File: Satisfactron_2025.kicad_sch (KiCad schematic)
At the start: 93 parts, among them J10 Conn_01x02, J11 Conn_01x03, J17 Conn_01x02, J18 Conn_01x02, J19 Conn_01x02, J4 65100516121, J5 Conn_01x05, J6 Conn_01x06, J7 Conn_01x02, J8 Conn_01x04, J9 Conn_01x02, Q2 G2302, SW1 SW_DPST_x2, SW2 SW_Push, SW5 SW_Push, SW6 SW_Push, SW7 SW_Push, U1 AMS1117-3.3, U2 TPS82130, U3 ESP32-S3-WROOM-1-N16R8

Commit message: Start populate schematics
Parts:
- removed C1, C24, C3, C5, C6: 100nF, Capacitor_SMD:C_0603_1608Metric_Pad1.08x0.95mm_HandSolder, symbol Device:C
- removed J10, J17, J18, J19, J9: Conn_01x02, Connector_PinHeader_2.54mm:PinHeader_1x02_P2.54mm_Vertical, symbol Connector_Generic:Conn_01x02
- removed J4: 65100516121, ConnectorsEvo:USB_Mini-B_Wuerth_65100516121_Horizontal, symbol Connector:USB_B_Mini
- removed J5: Conn_01x05, Connector_PinHeader_2.54mm:PinHeader_1x05_P2.54mm_Vertical, symbol Connector_Generic:Conn_01x05
- removed J7: Conn_01x02, Connector_Wire:SolderWire-0.75sqmm_1x02_P4.8mm_D1.25mm_OD2.3mm, symbol Connector_Generic:Conn_01x02
- removed R21, R22, R4, R5, R8: 10k, Resistor_SMD:R_0603_1608Metric_Pad0.98x0.95mm_HandSolder, symbol Device:R
- removed SW1: SW_DPST_x2, SW_Slide_SPDT_Straight_CK_OS102011MS2Q, symbol Switch:SW_SPDT_321
- added H10, H11, H12, H13, H14, H15, H16, H17, H18, H19, H5, H6, H7, H8, H9: SMTSO3040CTJ, Fastener_KSL:SMD-1_BD5.5-D4.0, symbol Fastener_KSL:SMTSO3040CTJ
- added J1: USB-TYPE-C-018, Connector_KSL:USB-C_SMD-TYPE-C-31-M-12, symbol Connector_KSL:USB-TYPE-C-018
- added J2: GT-BTP30002-0350B-019B, Connector_KSL:CONN-SMD_GT-BTP30002-0350B-019B, symbol Connector_KSL:GT-BTP30002-0350B-019B
- added SW1: SS-12D11G5R, Switch_KSL:SW-TH_SS-12D11G5R, symbol Switch_KSL:SS-12D11G5R
- added SW10, SW3, SW4, SW8, SW9: SPVN310101, Switch_KSL:SW-SMD_SPVN310101, symbol Switch_KSL:SPVN310101
- added U4, U5, U6, U7, U8: TSSP77038TR, Sensor_KSL:SENSOR-SMD_TSOP75238TR, symbol Sensor_KSL:TSSP77038TR
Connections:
- no-connect marks 8 -> 24
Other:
- note added: "Battery input (Canon LP-E17, 7.4V), main switch"
- note added: "IR reflective sensors"
- note added: "Mechanical"
- note added: "Micro-switches"
- note added: "USB input"
- note removed: "+ switch principal"
- note removed: "5V USB non connecté, utiliser avec PAMI sous tension"
- note removed: "Capteur fin de course (NC)"
- note removed: "Capteur infrarouge"
- note removed: "Entree batterie LP-E6P 7.4V"
- note removed: "Entree: USB"
- note removed: "ajouter capteur IR: C499566"
- note removed: "conn. 'USB' dupont"
- note removed: "rempl par pogo batterie"
- moved on the sheet: C8

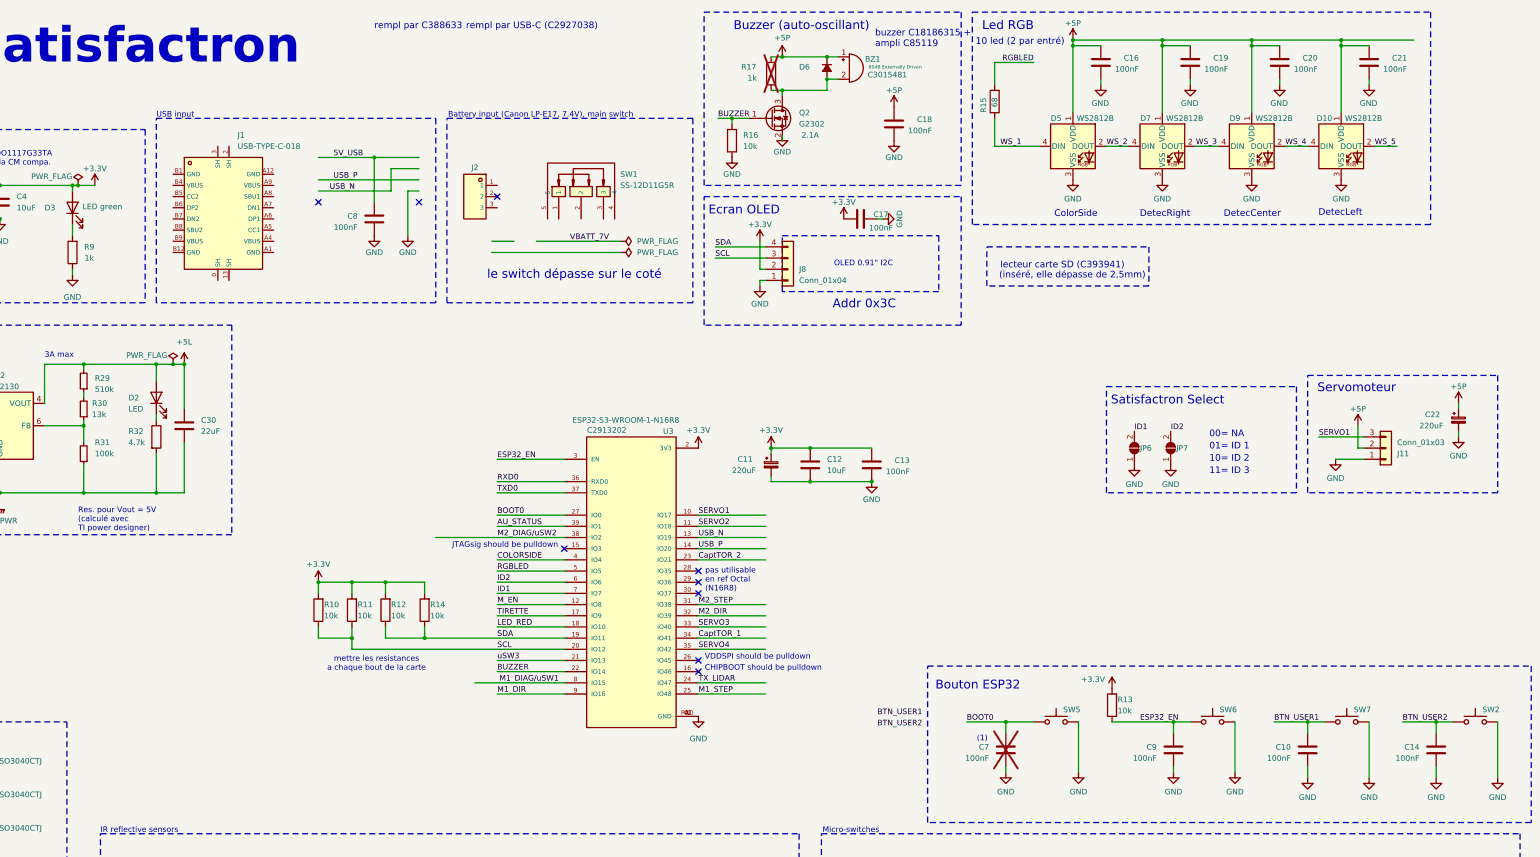
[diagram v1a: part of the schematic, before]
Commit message: Add DXF, sch placement + start PCB placement
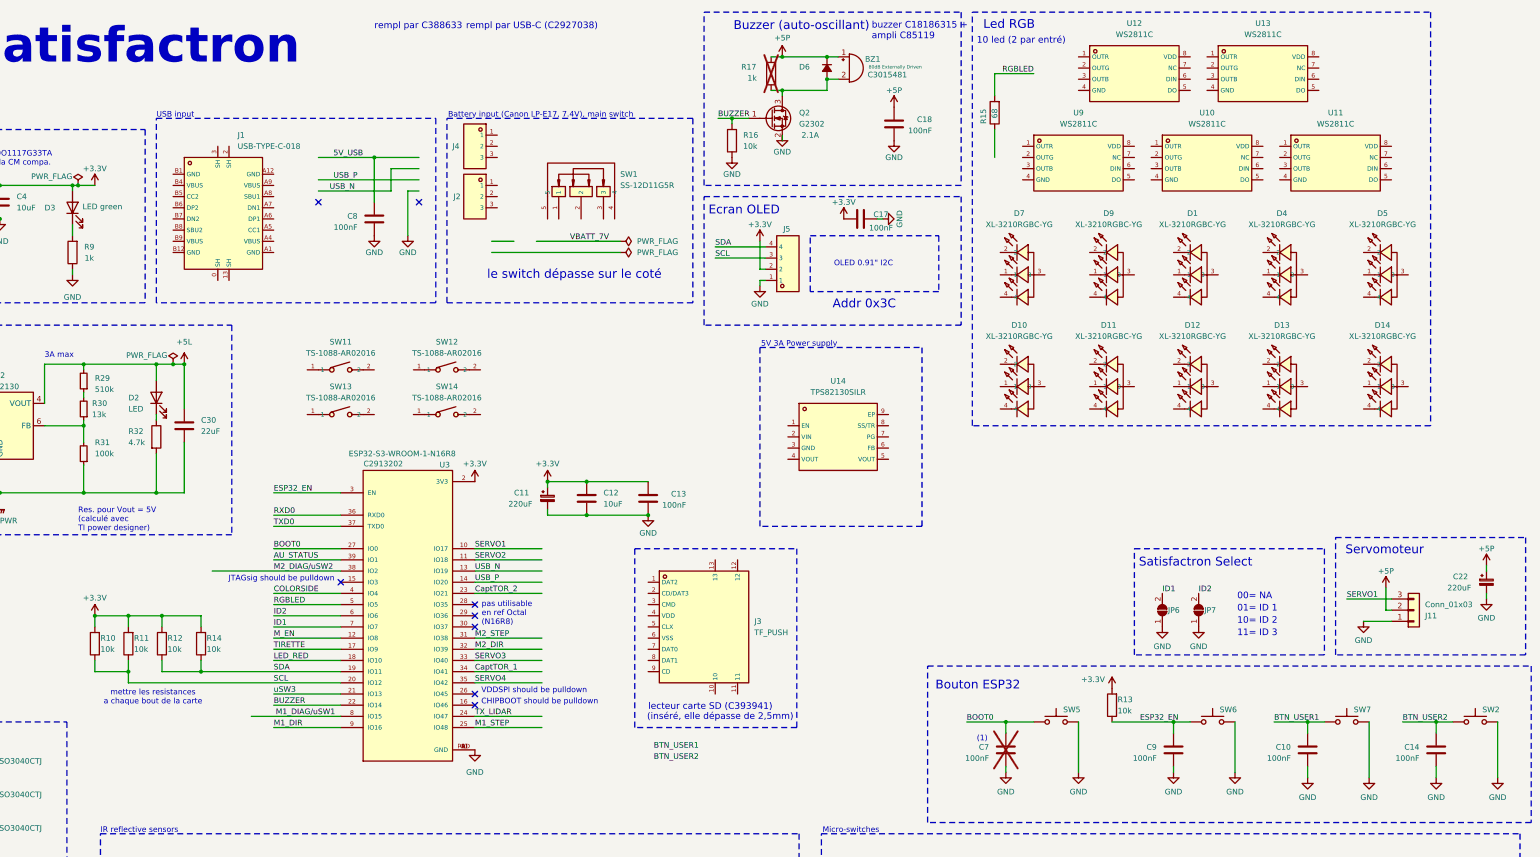
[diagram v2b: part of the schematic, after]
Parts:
- removed C16, C19, C20, C21: 100nF, Capacitor_SMD:C_0603_1608Metric_Pad1.08x0.95mm_HandSolder, symbol Device:C
- removed D10, D5, D7, D9: WS2812B, LED_SMD:LED_WS2812B_PLCC4_5.0x5.0mm_P3.2mm, symbol LED:WS2812B
- removed J8: Conn_01x04, Carte_Mere_PAMI_2025:Ecran_OLED0.9_Waveshare, symbol Connector_Generic:Conn_01x04
- added D1, D10, D11, D12, D13, D14, D4, D5, D7, D9: XL-3210RGBC-YG, LED_KSL:LED-ARRAY-SMD_HS-1204-RGB, symbol LED_KSL:XL-3210RGBC-YG
- added J3: TF_PUSH, Connector_KSL:TF-SMD_TF-PUSH, symbol Connector_KSL:TF_PUSH
- added J4: GT-BTP30002-0350B-019B, Connector_KSL:CONN-SMD_GT-BTP30002-0350B-019B, symbol Connector_KSL:GT-BTP30002-0350B-019B
- added J5: PZ254V-11-04P_C2691448, Connector_KSL:HDR-TH_4P-P2.54-V-M, symbol Connector_KSL:PZ254V-11-04P_C2691448
- added SW11, SW12, SW13, SW14: TS-1088-AR02016, Switch_KSL:SW-SMD_L3.9-W3.0-P4.45, symbol Switch_KSL:TS-1088-AR02016
- added U10, U11, U12, U13, U9: WS2811C, LED_Driver_KSL:SOP-8_L4.9-W3.9-P1.27-LS6.0-BL, symbol LED_Driver_KSL:WS2811C
- added U14: TPS82130SILR, DC-DC_converter_KSL:USIP-8_L3.0-W2.8-P0.65-TL-EP, symbol DC-DC_converter_KSL:TPS82130SILR
- U3: footprint Carte_Mere_PAMI_2025:ESP32-S3-WROOM-1-N16R8 -> MCU_KSL:WIRELM-SMD_ESP32-S3-WROOM-1
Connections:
- net +3.3V: now also J5.2
- net GND: now also J5.1
- net SCL: now also J5.3
- net SDA: now also J5.4
- net WS_1: no longer names the net of R15.1
- no-connect marks 24 -> 23
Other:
- note added: "5V 3A Power supply"
- note removed: "ColorSide"
- note removed: "DetecCenter"
- note removed: "DetecLeft"
- note removed: "DetecRight"
- company: Fait Tes Vacance -> (none)
- moved on the sheet: C11, C12, C13, C22, J11, JP6, JP7, R10, R11, R12, R14, R15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

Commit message: Continue PCB placement
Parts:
- removed SW1: SS-12D11G5R, Switch_KSL:SW-TH_SS-12D11G5R, symbol Switch_KSL:SS-12D11G5R
- removed U14: TPS82130SILR, DC-DC_converter_KSL:USIP-8_L3.0-W2.8-P0.65-TL-EP, symbol DC-DC_converter_KSL:TPS82130SILR
- added J10, J7, J8, J9: GT-BTP30002-0350B-019B, Connector_KSL:CONN-SMD_GT-BTP30002-0350B-019B, symbol Connector_KSL:GT-BTP30002-0350B-019B
- added SW1: MSK-22D18G4_051, Switch_KSL:SW-TH_HX-MSK-22D18G4-051, symbol Switch_KSL:MSK-22D18G4_051
- J5: footprint Connector_KSL:HDR-TH_4P-P2.54-V-M -> Screen_KSL:Waveshare_screen_0.9
- U2: footprint 12V-actuators_pcb:MicroSiP -> DC-DC_converter_KSL:USIP-8_L3.0-W2.8-P0.65-TL-EP
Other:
- note added: "Buttons"
- note removed: "5V 3A Power supply"
- note removed: "rempl par C388633"
- note removed: "rempl par USB-C (C2927038)"
- moved on the sheet: J2, J4

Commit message: avancement schema
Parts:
- removed BZ1: Buzzer, Buzzer_Beeper:Buzzer_TDK_PS1240P02BT_D12.2mm_H6.5mm, symbol Device:Buzzer
- removed C18: 100nF, Capacitor_SMD:C_0603_1608Metric_Pad1.08x0.95mm_HandSolder, symbol Device:C
- removed D6: 1N4148W, Diode_SMD:D_SOD-123F, symbol Device:D_Small_Filled
- removed H10, H11, H12, H13, H14, H15, H16, H17, H18, H19, H5, H6, H7, H8, H9: SMTSO3040CTJ, Fastener_KSL:SMD-1_BD5.5-D4.0, symbol Fastener_KSL:SMTSO3040CTJ
- removed Q2: G2302, Package_TO_SOT_SMD:SOT-23, symbol Device:Q_NMOS_GSD
- removed R15: 68, Resistor_SMD:R_0603_1608Metric_Pad0.98x0.95mm_HandSolder, symbol Device:R
- removed R16: 10k, Resistor_SMD:R_0603_1608Metric_Pad0.98x0.95mm_HandSolder, symbol Device:R
- removed R17, R9: 1k, Resistor_SMD:R_0603_1608Metric_Pad0.98x0.95mm_HandSolder, symbol Device:R
- removed R26: 10k, Resistor_SMD:R_0603_1608Metric, symbol Device:R_Small
- removed R32: 4.7k, Resistor_SMD:R_0603_1608Metric, symbol Device:R
- removed SW11, SW12, SW13, SW14: TS-1088-AR02016, Switch_KSL:SW-SMD_L3.9-W3.0-P4.45, symbol Switch_KSL:TS-1088-AR02016
- added D15: 1N4148W, Diode_SMD:D_SOD-123F, symbol Device:D_Small_Filled
- added H10, H11, H12, H13, H14, H15, H5, H6, H7, H8, H9: SMTSO3040CTJ, Fastener_KSL:SMD-1_BD5.5-D4.0, symbol Mechanical:MountingHole_Pad
- added R1, R3: 5.1k, Resistor_SMD:R_0603_1608Metric, symbol Device:R_Small
- added R2: 4.7k, Resistor_SMD:R_0603_1608Metric, symbol Device:R_Small
- added R4: 1k, Resistor_SMD:R_0603_1608Metric, symbol Device:R_Small
- added R5, R6: 68, Resistor_SMD:R_0603_1608Metric, symbol Device:R_Small
- added SW11, SW12, SW13, SW14, SW15: SPVN310101, Switch_KSL:SW-SMD_SPVN310101, symbol Switch_KSL:SPVN310101
- H1, H2, H3, H4: value MountingHole_Pad -> SMTSO3040CTJ; footprint MountingHole:MountingHole_3.2mm_M3_Pad -> Fastener_KSL:SMD-1_BD5.5-D4.0; LCSC (none) -> C2915635; now in the parts list
- J2, J4: now not fitted; now left out of the parts list
- R27: now fitted; now in the parts list
- SW2, SW5, SW6, SW7: value SW_Push -> TS-1088-AR02016; footprint SW_Push_1TS009xxxx-xxxx-xxxx_6x6x5mm -> Switch_KSL:SW-SMD_L3.9-W3.0-P4.45; LCSC (none) -> C720477; Mouser 710-430133050816 -> (none)
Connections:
- net +5VP is gone; now on net +5L: R28.1
- net 5V_USB is gone; now on net VBUS: C8.1
- net GNDPWR is gone; now on net GND: C25.2, C29.2, C30.2, R27.1, R31.1, U2.3 (GND), U2.9 (GND)
- net +5L: now also JP1.1 (A), D15.1 (K); no longer JP1.3 (B)
- net GND: now also J1.0 (SH), J1.13 (SH), J1.2 (SH), J1.3 (SH), J1.A1 (GND), J1.A12 (GND), J1.B1 (GND), J1.B12 (GND), J2.2, SW10.2, SW10.3, SW3.2, SW3.3, SW4.2, SW4.3, SW8.2, SW8.3, SW9.2, SW9.3, H10.1, H11.1, H12.1, H13.1, H14.1, H15.1, H5.1, H6.1, H7.1, H8.1, H9.1, R1.1, R2.1, R3.1, R4.1, SW11.2, SW11.3, SW12.2, SW12.3, SW13.2, SW13.3, SW14.2, SW14.3, SW15.2, SW15.3
- net RGBLED: now also R5.2
- net USB_N: now also J1.A7 (DN1), J1.B7 (DN2)
- net USB_P: now also J1.A6 (DP1), J1.B6 (DP2)
- net VBATT_7V: now also J4.1, SW1.1, SW1.2, SW1.4, SW1.5; no longer JP1.1 (A)
- net uSW1: now also SW3.1, SW3.4, SW4.1, SW4.4
- net uSW2: now also SW8.1, SW8.4, SW9.1, SW9.4
- net uSW3: now also SW10.1, SW10.4, SW11.1, SW11.4
- net uSW4: now also SW12.1, SW12.4, SW13.1, SW13.4
- net uSW5: now also SW14.1, SW14.4, SW15.1, SW15.4
- net EN_5L: now reaches R27.2, U2.1 (EN)
- net EN_5L: now also R6.1
- net at D2.1 (K): now also R2.2
- net VBUS: now reaches J1.A4 (VBUS)
- net VBUS: now also J1.A9 (VBUS), J1.B4 (VBUS), J1.B9 (VBUS), D15.2 (A)
- net CC1: now reaches J1.A5 (CC1)
- net CC1: now also R3.2
- net CC2: now reaches J1.B5 (CC2)
- net CC2: now also R1.2
- net at D3.1 (K): now also R4.2
- net SWITCHED_7V: now reaches SW1.3
- net SWITCHED_7V: now also JP1.3 (B), SW1.6, R6.2
- no-connect marks 23 -> 24
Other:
- note added: "Alim 5V - 3A (max)"
- note added: "Battery input (Canon LP-E17, 7.4V)"
- note added: "Main Switch (a actionner avec un outil)"
- note added: "USB C input"
- note added: "composant de spare"
- note added: "entretoise soudée de montage"
- note removed: "3A max"
- note removed: "Alim 5V"
- note removed: "Battery input (Canon LP-E17, 7.4V), main switch"
- note removed: "Buttons"
- note removed: "Buzzer (auto-oscillant)"
- note removed: "Mechanical"
- note removed: "Trous de montage"
- note removed: "USB input"
- note removed: "ajouter des tabs de 3mm de large sur le pourtour pour emboiter dans la struct."
- note removed: "ajuster nombre"
- note removed: "buzzer C18186315 + ampli C85119"
- note removed: "entretoise soudé M3x3, en BOT"
- note removed: "le switch dépasse sur le coté"
- moved on the sheet: C10, C11, C12, C13, C14, C15, C17, C2, C22, C23, C25, C26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

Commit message: Schematics done 90% + PCB placement +10%
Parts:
- added C1, C16, C3, C5, C6: 22uF, Capacitor_SMD:C_0805_2012Metric, symbol Device:C
- added C18, C19, C20, C21, C24: 100n, symbol Device:C_Small
- added R15, R16, R17, R8, R9: 150, Resistor_SMD:R_0603_1608Metric, symbol Device:R_Small
- R5: value 68 -> 33
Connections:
- net COLORSIDE is gone; now on net RGBLED: U3.4 (IO4)
- net CaptTOR_1 is gone; now on net IRSENS_4: U3.34 (IO41)
- net CaptTOR_2 is gone; now on net ID2: U3.23 (IO21)
- net M2_DIR is gone; now on net IRSENS_2: U3.32 (IO39)
- net M2_STEP is gone; now on net IRSENS_1: U3.31 (IO38)
- net M_EN is gone; now on net CS: U3.12 (IO8)
- net SERVO2 is gone; now on net ID1: U3.11 (IO18)
- net SERVO3 is gone; now on net IRSENS_3: U3.33 (IO40)
- net SERVO4 is gone; now on net IRSENS_5: U3.35 (IO42)
- net TIRETTE is gone; now on net CARD_DETECT: U3.17 (IO9)
- net +3.3V: now also J3.4 (VDD), U4.2 (+VS), U5.2 (+VS), U6.2 (+VS), U7.2 (+VS), U8.2 (+VS), C1.1, C16.1, C3.1, C5.1, C6.1
- net +5L: now also D1.3 (+), D10.3 (+), D11.3 (+), D12.3 (+), D13.3 (+), D14.3 (+), D4.3 (+), D5.3 (+), D7.3 (+), D9.3 (+), R15.2, R16.2, R17.2, R8.2, R9.2
- net GND: now also J3.10, J3.11, J3.12, J3.13, J3.6 (VSS), U10.4 (GND), U11.4 (GND), U12.4 (GND), U13.4 (GND), U4.1 (GND), U4.4 (GND), U5.1 (GND), U5.4 (GND), U6.1 (GND), U6.4 (GND), U7.1 (GND), U7.4 (GND), U8.1 (GND), U8.4 (GND), U9.4 (GND), C1.2, C16.2, C18.1, C19.1, C20.1, C21.1, C24.1, C3.2, C5.2, C6.2
- net ID1: no longer U3.7 (IO7)
- net ID2: no longer U3.6 (IO6)
- net RGBLED: now also R5.1; no longer R5.2, U3.5 (IO5)
- net at U10.1 (OUTR): now also D5.4 (R), D7.4 (R)
- net at U10.2 (OUTG): now also D5.2 (G), D7.2 (G)
- net at U10.3 (OUTB): now also D5.1 (B), D7.1 (B)
- net at U10.5 (DO): now also U11.6 (DIN)
- net at U10.6 (DIN): now also U9.5 (DO)
- net at U10.8 (VDD): now also C18.2, R9.1
- net IRSENS_4: now reaches U7.3 (OUT)
- net at U9.1 (OUTR): now also D1.4 (R), D4.4 (R)
- net at U9.2 (OUTG): now also D1.2 (G), D4.2 (G)
- net at U9.3 (OUTB): now also D1.1 (B), D4.1 (B)
- net at U9.6 (DIN): now also R5.2
- net at U9.8 (VDD): now also C24.2, R8.1
- net CS: now reaches J3.2 (CD/DAT3)
- net MOSI: now reaches J3.3 (CMD)
- net MOSI: now also U3.6 (IO6)
- net SCK: now reaches J3.5 (CLX)
- net SCK: now also U3.5 (IO5)
- net MISO: now reaches J3.7 (DAT0)
- net MISO: now also U3.7 (IO7)
- net CARD_DETECT: now reaches J3.9 (CD)
- net at U13.1 (OUTR): now also D13.4 (R), D14.4 (R)
- net at U13.2 (OUTG): now also D13.2 (G), D14.2 (G)
- net at U13.3 (OUTB): now also D13.1 (B), D14.1 (B)
- net at U13.6 (DIN): now also U12.5 (DO)
- net at U13.8 (VDD): now also C21.2, R17.1
- net IRSENS_5: now reaches U8.3 (OUT)
- net at U11.1 (OUTR): now also D10.4 (R), D9.4 (R)
- net at U11.2 (OUTG): now also D10.2 (G), D9.2 (G)
- net at U11.3 (OUTB): now also D10.1 (B), D9.1 (B)
- net at U11.5 (DO): now also U12.6 (DIN)
- net at U11.8 (VDD): now also C19.2, R15.1
- net IRSENS_2: now reaches U5.3 (OUT)
- net at U12.1 (OUTR): now also D11.4 (R), D12.4 (R)
- net at U12.2 (OUTG): now also D11.2 (G), D12.2 (G)
- net at U12.3 (OUTB): now also D11.1 (B), D12.1 (B)
- net at U12.8 (VDD): now also C20.2, R16.1
- net IRSENS_3: now reaches U4.3 (OUT)
- net IRSENS_1: now reaches U6.3 (OUT)
- net BUZZER: no longer names the net of U3.22 (IO14)
- no-connect marks 24 -> 32
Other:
- note added: "10 led (2 per driver)"
- note added: "RGB LED"
- note added: "SD card reader"
- note added: "Satisfactron PCB"
- note removed: "(inséré, elle dépasse de 2,5mm)"
- note removed: "10 led (2 par entré)"
- note removed: "Carte Satisfactron"
- note removed: "Led RGB"
- note removed: "lecteur carte SD (C393941)"
- moved on the sheet: D1, D10, D11, D12, D13, D14, D4, D5, D7, D9, J3, R5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
